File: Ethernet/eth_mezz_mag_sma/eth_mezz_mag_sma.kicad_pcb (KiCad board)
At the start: 2 copper layers, 50 x 41 mm, 13 parts, among them J1 Conn_01x09_Male, J2 TX-, J3 RX+, J4 RX-, J5 TX+

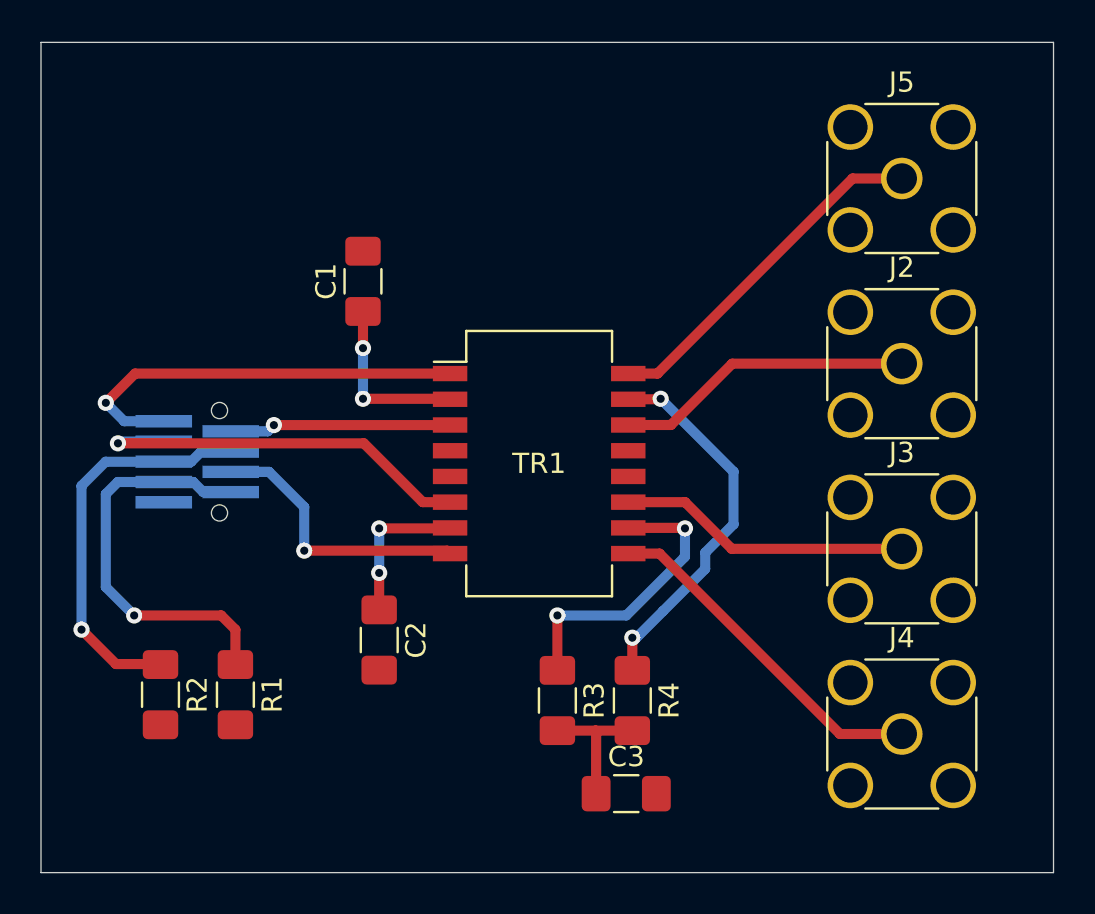
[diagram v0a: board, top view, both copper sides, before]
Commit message: PHY module with RJ45
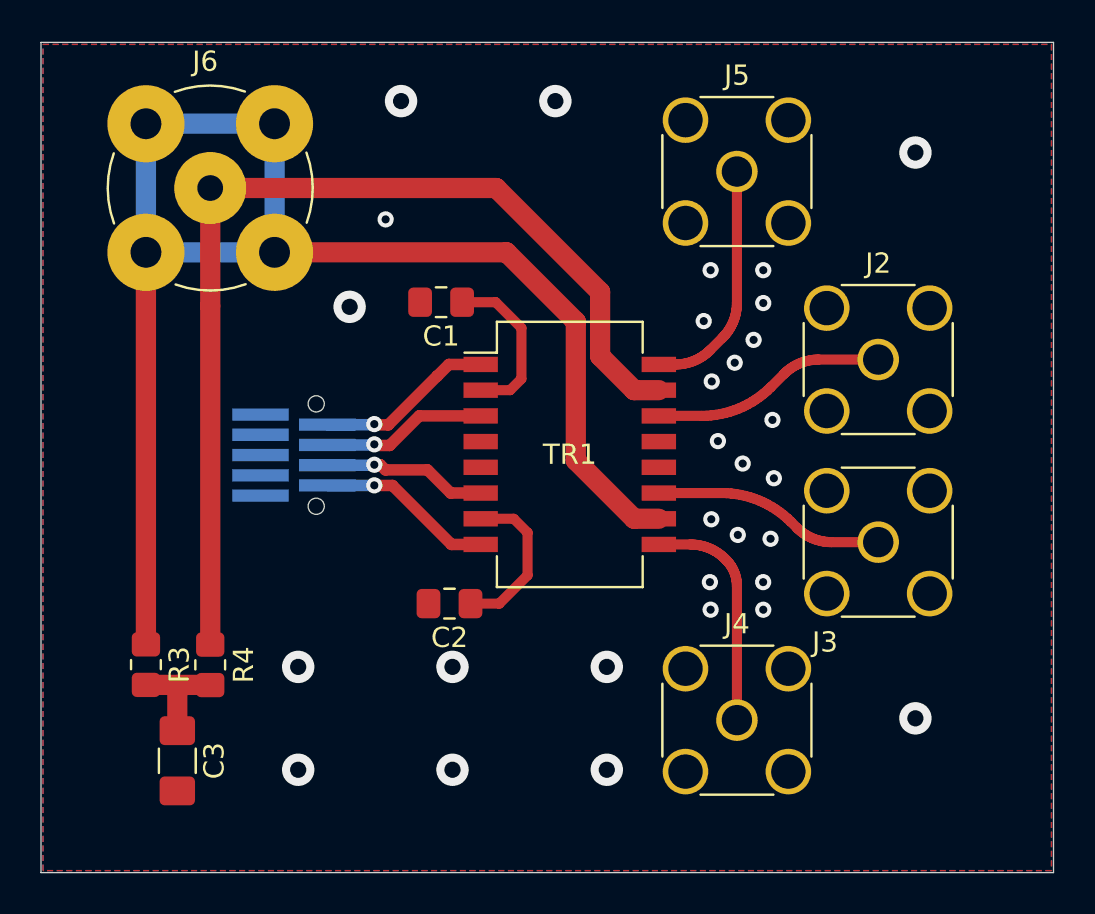
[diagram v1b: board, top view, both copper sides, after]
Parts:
- removed R1, R2: 75R, Resistor_SMD:R_1206_3216Metric_Pad1.42x1.75mm_HandSolder
- added J6: Conn_Coaxial, Connector_Coaxial:BNC_TEConnectivity_1478204_Vertical, F.Cu at (105.4, 63.2)
- C1, C2: footprint Resistor_SMD:R_1206_3216Metric_Pad1.42x1.75mm_HandSolder -> Capacitor_SMD:C_0805_2012Metric_Pad1.18x1.45mm_HandSolder
- R3, R4: footprint Resistor_SMD:R_1206_3216Metric_Pad1.42x1.75mm_HandSolder -> Resistor_SMD:R_0805_2012Metric_Pad1.20x1.40mm_HandSolder
- moved C3 22.2 mm to (103.7, 91.5), turned to 270 degrees
- moved R4 20.9 mm to (105.4, 86.7)
- moved R3 20.4 mm to (102.2, 86.7)
- moved J4 8.17 mm to (131.4, 89.5)
- moved J5 8.15 mm to (131.4, 62.4)
- moved J1 4.79 mm to (118.8, 90.4)
- moved C1 3.99 mm to (116.8, 68.8), turned to 180 degrees
- moved C2 3.91 mm to (117.2, 83.7), turned to 180 degrees
- moved TR1 1.58 mm to (123.1, 76.3)
- moved J3 1.21 mm to (138.3, 80.7)
- moved J2 1.18 mm to (138.3, 71.7)
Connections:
- net /RX+out renamed /RXout+
- net /RX-out renamed /RXout-
- net /TX+out renamed /TXout+
- net /TX-out renamed /TXout-
- J1 pad 1: /TX+in -> GND
- J1 pad 2: /TX-in -> /TXin+
- J1 pad 3: /RX+in -> GND
- J1 pad 4: Net-(J1-Pad4) -> /TXin-
- J1 pad 5: Net-(J1-Pad4) -> GND
- J1 pad 6: /RX-in -> /RXin+
- J1 pad 7: Net-(J1-Pad7) -> GND
- J1 pad 8: Net-(J1-Pad7) -> /RXin-
- TR1 pad 1: /TX+in -> /TXin+
- TR1 pad 3: /TX-in -> /TXin-
- TR1 pad 6: /RX+in -> /RXin+
- TR1 pad 8: /RX-in -> /RXin-
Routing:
- net Net-(J6-Pad2): track 14.4 -> 73.2 mm, vias 2 -> 0
- net Net-(J6-Pad1): track 18.7 -> 50.7 mm, vias 2 -> 0
- net /TX+in: track 20.8 -> 0.00 mm, vias 1 -> 0
- net Net-(J1-Pad7): track 20.2 -> 0.00 mm, vias 1 -> 0
- net /RX+in: track 19.9 -> 0.00 mm, vias 1 -> 0
- net Net-(J1-Pad4): track 19.8 -> 0.00 mm, vias 1 -> 0
- net /RX-in: track 13.8 -> 0.00 mm, vias 1 -> 0
- net /TX-in: track 11.0 -> 0.00 mm, vias 1 -> 0
- net /TXin+: track 0.00 -> 8.81 mm, vias 0 -> 1
- net /RXin-: track 0.00 -> 8.78 mm, vias 0 -> 1
- net /TXin-: track 0.00 -> 8.25 mm, vias 0 -> 1
- net /RXin+: track 0.00 -> 8.16 mm, vias 0 -> 1
- net /RXout-: track 17.2 -> 11.6 mm
- net /TXout+: track 17.5 -> 12.0 mm
- net /TXout-: track 14.8 -> 11.7 mm
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- added copper zone on B.Cu, net GND
- added copper zone on F.Cu, net GND
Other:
- net class Diff added: clearance 0.2, trace_width 0.5, via_dia 0.8, via_drill 0.4

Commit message: SomeBoardsReady
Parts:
- added H1: MountingHole_Pad, MountingHole:MountingHole_3.2mm_M3_Pad_Via, F.Cu at (103.1, 89.3)
- added H2: MountingHole_Pad, MountingHole:MountingHole_3.2mm_M3_Pad_Via, F.Cu at (103.1, 63.5)
- moved C3 36.3 mm to (123.2, 60.9), turned to 90 degrees
- moved R3 29.0 mm to (122.1, 65.6), turned to 90 degrees
- moved R4 28.3 mm to (124.2, 65.6), turned to 90 degrees
- moved C2 15.5 mm to (102.6, 78.4)
- moved C1 15.2 mm to (102.6, 74.3)
- moved J6 8.64 mm to (114.0, 63.2)
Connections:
- C1 pad 1: Net-(C1-Pad1) -> /TCT
- C2 pad 1: Net-(C2-Pad1) -> /RCT
- J1 pad 1: GND -> /TCT
- J1 pad 9: GND -> /RCT
- TR1 pad 2: Net-(C1-Pad1) -> /TCT
- TR1 pad 7: Net-(C2-Pad1) -> /RCT
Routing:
- net /RCT: track 0.00 -> 30.1 mm, vias 0 -> 1
- net /TCT: track 0.00 -> 28.6 mm, vias 0 -> 1
- net Net-(J6-Pad2): track 73.2 -> 46.4 mm
- net Net-(J6-Pad1): track 50.7 -> 23.9 mm, vias 0 -> 2
- net Net-(C1-Pad1): track 8.21 -> 0.00 mm
- net Net-(C2-Pad1): track 8.11 -> 0.00 mm
- net Net-(C3-Pad1): track 5.46 -> 4.42 mm
